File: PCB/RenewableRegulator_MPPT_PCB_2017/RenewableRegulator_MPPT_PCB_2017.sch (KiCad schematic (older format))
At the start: 35 parts, among them J1 TEMP, J2 Arduino_Nano, P1 INPUT, P2 Vref?, P3 MicroSD, P4 A6_7, P5 OUTPUT, P6 SERIAL, P7 A2, P8 TP_Vin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

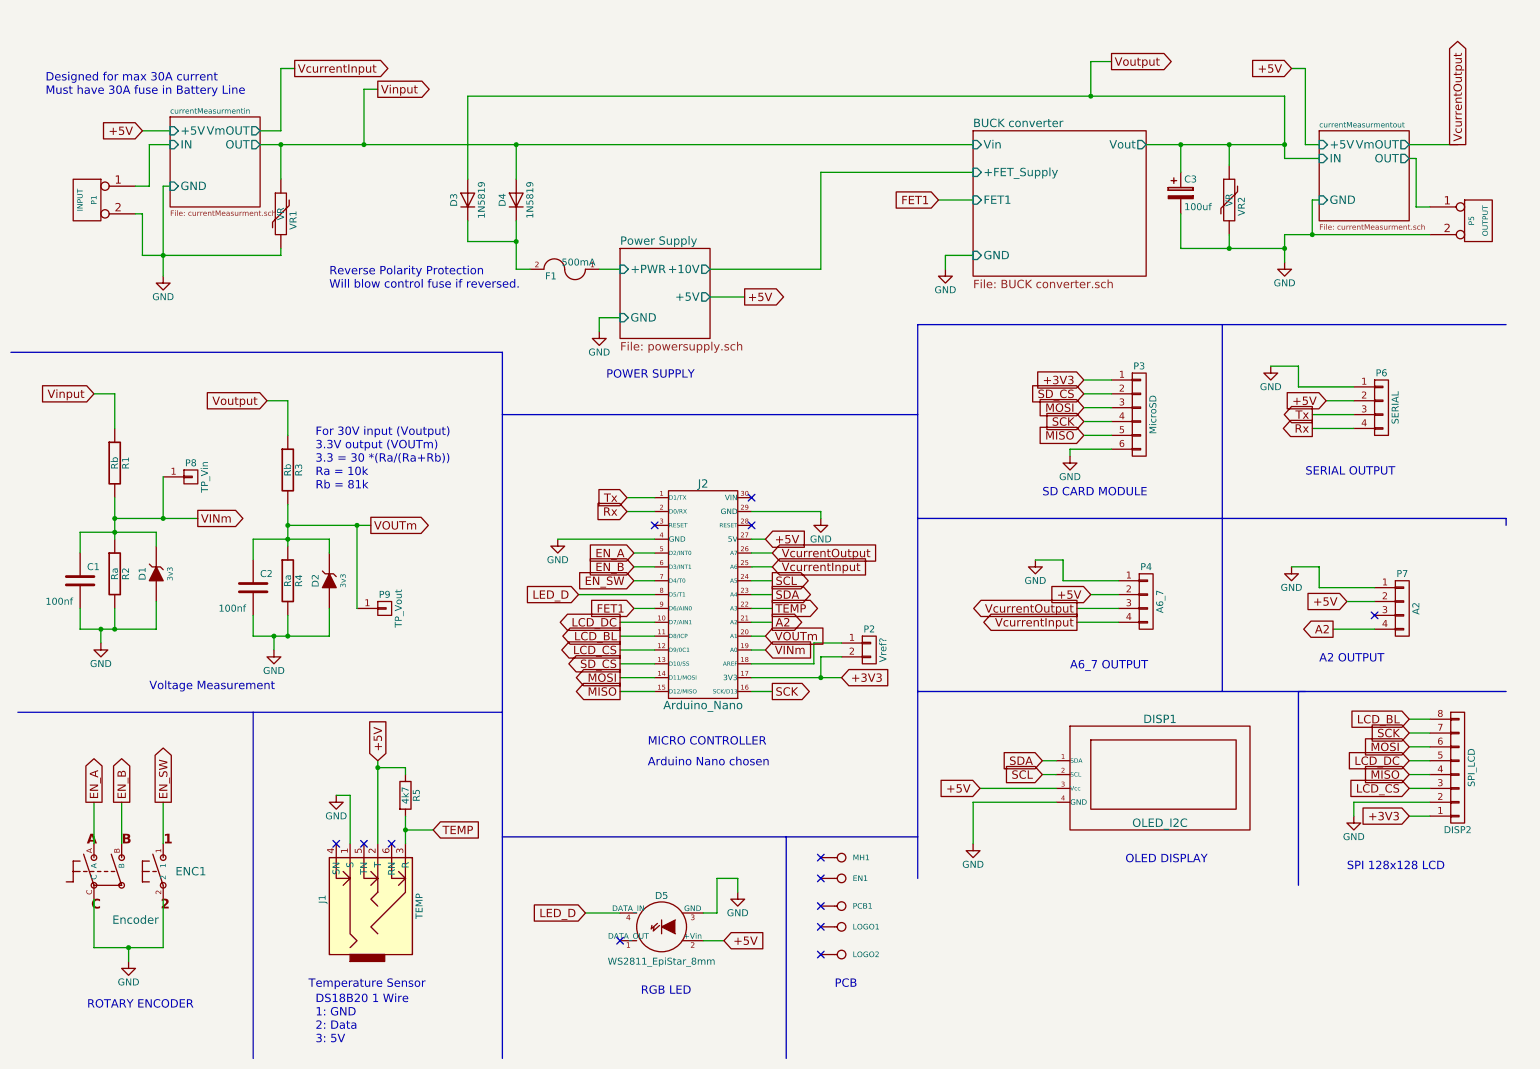
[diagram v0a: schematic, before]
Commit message: First version MPPT PCB
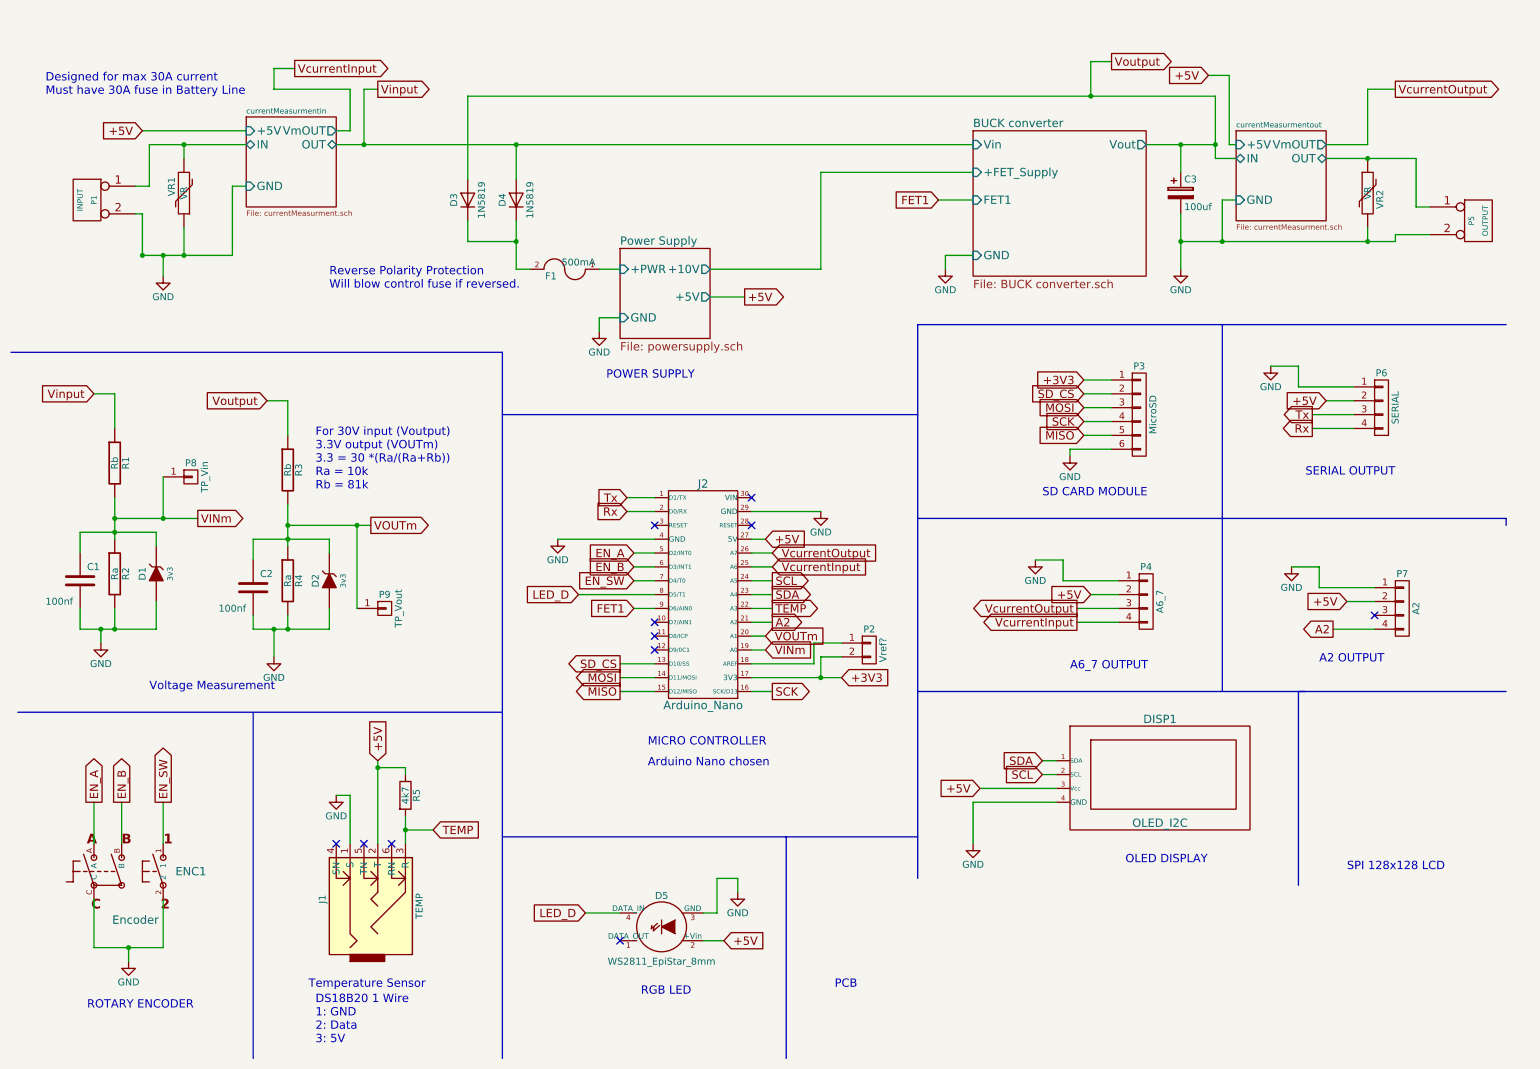
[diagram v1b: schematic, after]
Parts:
- removed DISP2: SPI_LCD, REInnovationFootprint:TH_LCD_SPI_128x128, symbol CONN_01X08
- removed EN1: PCB, symbol CONN_1
- removed LOGO1: LOGO, CuriousElectric3:CEC_Globe_10mm_FCU, symbol CONN_1
- removed LOGO2: LOGO, CuriousElectric3:TCEC_Words_13mm, symbol CONN_1
- removed MH1: Mounting holes, symbol CONN_1
- removed PCB1: PCB, REInnovationFootprint:PCB_75x100mm, symbol CONN_1
- C1, C2: footprint matts_components:C1_wide_lg_pad -> REInnovationFootprint:cond_1
- P8: footprint matts_components:1pin_0_8mm -> REInnovationFootprint:tp
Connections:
- net GND: now also VR1.1; no longer VR1.2
- net Vinput: no longer VR1.1
- net Voutput: no longer VR2.1
- net currentMeasurmentin/IN: now also VR1.2
- net currentMeasurmentout/OUT: now also VR2.1
- net LCD_BL: no longer names the net of J2.11 (D8/ICP)
- net LCD_CS: no longer names the net of J2.12 (D9/0C1)
- net LCD_DC: no longer names the net of J2.10 (D7/AIN1)
- no-connect marks 13 -> 11
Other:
- moved on the sheet: VR1, VR2

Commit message: Updated MPPT PCB
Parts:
- P3: footprint matts_components:SIL-6_large_pads_marker -> REInnovationFootprint:SIL-6_large_pads_marker
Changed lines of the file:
@@
 F 0 "P3" H 8600 3500 50  0000 C CNN
 F 1 "MicroSD" V 8700 3150 50  0000 C CNN
-F 2 "matts_components:SIL-6_large_pads_marker" H 8600 3150 50  0001 C CNN
+F 2 "REInnovationFootprint:SIL-6_large_pads_marker" H 8600 3150 50  0001 C CNN
 F 3 "http://www.gearbest.com/development-boards/pp_63013.html?currency=GBP&vip=760169&gclid=CPHFuoqAjdMCFUK7GwodO08Omw" H 8600 3150 50  0001 C CNN
 F 4 "~" H 8600 3150 60  0000 C CNN "Notes"
